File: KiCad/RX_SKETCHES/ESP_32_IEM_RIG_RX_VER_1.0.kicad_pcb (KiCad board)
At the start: 2 copper layers, 64 parts, among them J1 AudioJack3, J6 USB_C_Receptacle_USB2.0_16P, Q1 S8050, Q2 S8050, SW2 Interpolation Mode, SW3 DAC Soft Mute, SW4 ON/OFF, U1 PCM5102, U2 ESP32-WROOM-32U, U3 MAX97220AETE_T, U4 LM3940IMPX-3.3_NOPB, U5 CP2102C-Axx-xQFN24

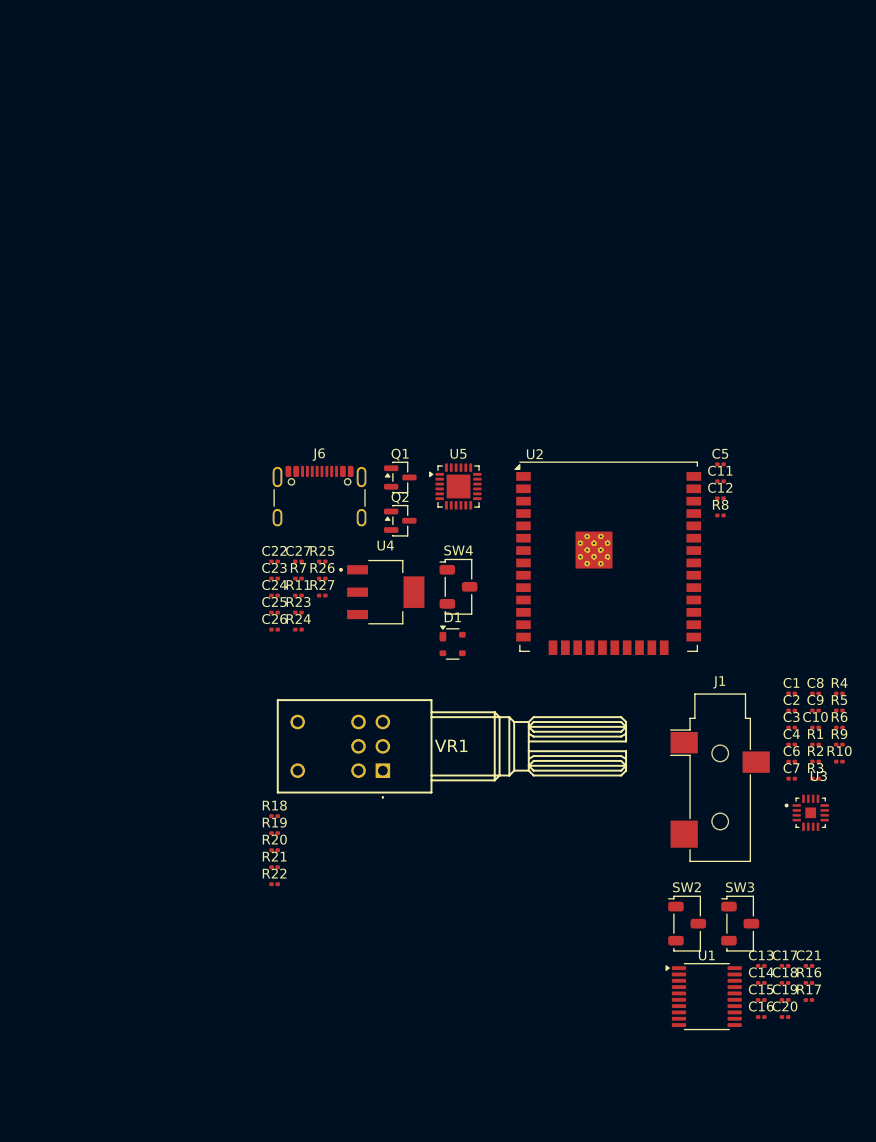
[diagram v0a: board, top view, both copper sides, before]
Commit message: RX v1: complete PCB layout, retune analog chain, fix ESD clamp placement
Brings the RX schematic and board up to a fabricable state. DRC is clean:
zero unconnected items, zero schematic-parity issues. The 16 remaining
violations are footprint-inherent and documented rather than worked around
(ESP32-WROOM thermal via array drilled 0.2 mm against a 0.3 mm rule, and
USB-C NPTH-to-pad spacing from the vendor land pattern).

Analog:
- Gain network populated at RF 4.7k / RIN 47k (-20 dB) rather than DNP 10k.
  Tames the PCM5102's 2.1 Vrms into sensitive IEMs, gives the 10k pot a
  4.7x loading ratio instead of 1:1, and lifts the coupling corner clear of
  the audible band.
- Coupling caps C1-C4 raised 0.47uF -> 1uF. Corner 7.2 Hz -> 3.4 Hz, and it
  halves the signal developed across the ceramic at 20 Hz, which is where
  Class-II dielectric distortion actually shows up.
- PCM5102 mode pins no longer float: 100k pulldowns on FLT and XSMT, with
  DEMP and FMT strapped to GND.

Power and protection:
- D1's third TVS channel moved off the switched +5V rail onto VBUS_RAW. An
  ESD clamp has to sit on the connector pin exposed to a finger; behind the
  power switch it disconnected exactly when the board is most likely to be
  handled. The off state is unaffected -- a TVS is open below its standoff
  voltage and SW4 still breaks the rail.
- All three slide switches now follow one rule: the open throw is the safe
  default (powered off / normal-latency filter / muted).

Housekeeping:
- C28 and mounting holes REF1-REF4 added to the schematic, clearing parity
  errors against parts that previously existed only on the PCB.
- Gain, loudness, and filter math written up in README.org with sources so
  the numbers can be re-derived; rationale logged in hardware_revisions.org.
- .gitignore now covers the editor .history/ directory and ESP-IDF build
  output, which were showing up as untracked noise.

Firmware and build artifacts are deliberately excluded from this commit.

Co-authored-b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
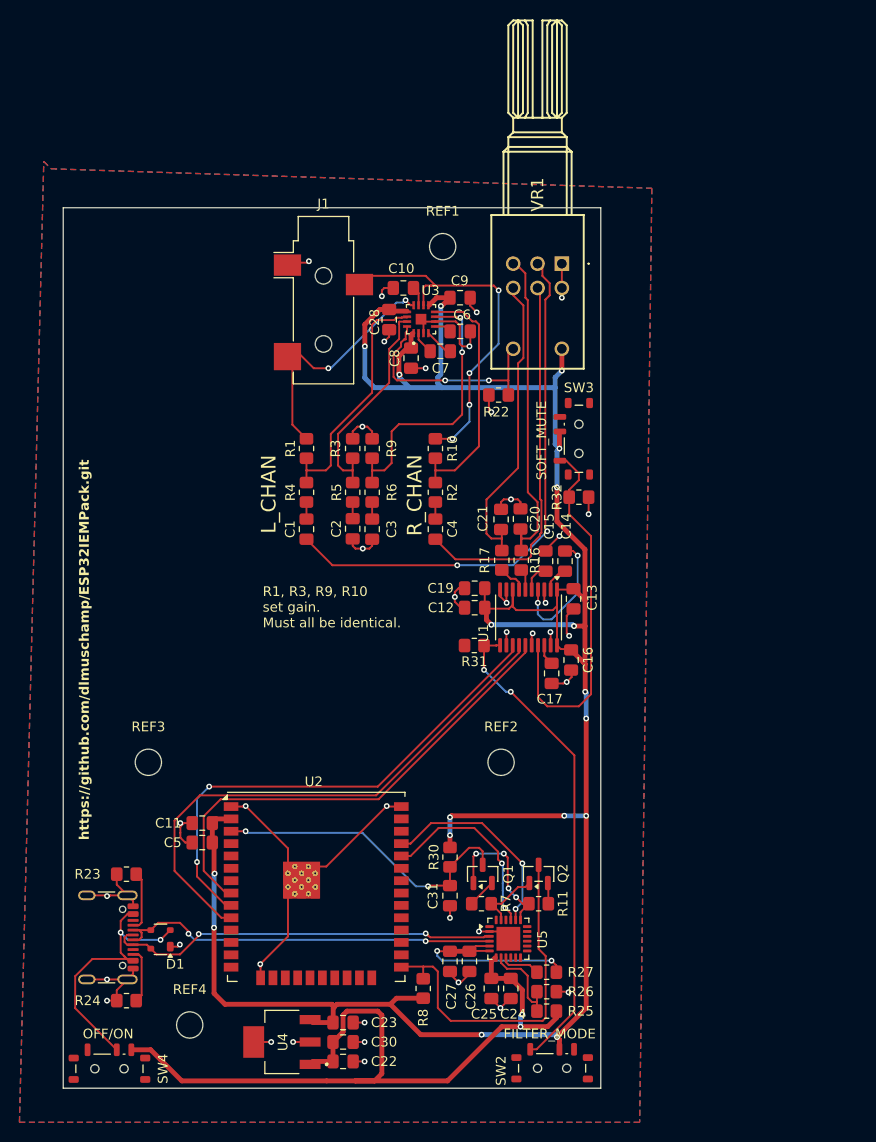
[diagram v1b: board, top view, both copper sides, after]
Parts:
- removed C18: 10u, Capacitor_SMD:C_0201_0603Metric
- removed R18, R20: 1k, Resistor_SMD:R_0201_0603Metric
- removed R19, R21: 10R, Resistor_SMD:R_0201_0603Metric
- added C28: 1u, Capacitor_SMD:C_0805_2012Metric_Pad1.18x1.45mm_HandSolder, F.Cu at (130.0, 50.0)
- added C30: 22u, Capacitor_SMD:C_0805_2012Metric_Pad1.18x1.45mm_HandSolder, F.Cu at (125.3, 124.2)
- added C31: 0.1u, Capacitor_SMD:C_0805_2012Metric_Pad1.18x1.45mm_HandSolder, F.Cu at (136.2, 109.2)
- added R30: 10k, Resistor_SMD:R_0805_2012Metric_Pad1.20x1.40mm_HandSolder, F.Cu at (136.2, 105.2)
- added R31: 100k, Resistor_SMD:R_0805_2012Metric_Pad1.20x1.40mm_HandSolder, F.Cu at (138.8, 83.5)
- added R32: 100k, Resistor_SMD:R_0805_2012Metric_Pad1.20x1.40mm_HandSolder, F.Cu at (149.5, 68.2)
- added REF1: MountingHole_2.7mm_M2.5, MountingHole:MountingHole_2.7mm_M2.5, F.Cu at (135.5, 42.5)
- added REF2: MountingHole_2.7mm_M2.5, MountingHole:MountingHole_2.7mm_M2.5, F.Cu at (141.5, 95.5)
- added REF3: MountingHole_2.7mm_M2.5, MountingHole:MountingHole_2.7mm_M2.5, F.Cu at (105.2, 95.5)
- added REF4: MountingHole_2.7mm_M2.5, MountingHole:MountingHole_2.7mm_M2.5, F.Cu at (109.5, 122.5)
- C1, C2, C3, C4: value 0.47u -> 1u; footprint Capacitor_SMD:C_0201_0603Metric -> Capacitor_SMD:C_0805_2012Metric_Pad1.18x1.45mm_HandSolder
- C10, C11, C13, C14, C15, C16, C17, C19, C20, C21, C23, C24, C25, C26, C27, C6, C7, C8, C9: footprint Capacitor_SMD:C_0201_0603Metric -> Capacitor_SMD:C_0805_2012Metric_Pad1.18x1.45mm_HandSolder
- C12: value 1u -> 10u; footprint Capacitor_SMD:C_0201_0603Metric -> Capacitor_SMD:C_0805_2012Metric_Pad1.18x1.45mm_HandSolder
- C22: value 22u -> 0.47u; footprint Capacitor_SMD:C_0201_0603Metric -> Capacitor_SMD:C_0805_2012Metric_Pad1.18x1.45mm_HandSolder
- C5: value 10u -> 22u; footprint Capacitor_SMD:C_0201_0603Metric -> Capacitor_SMD:C_0805_2012Metric_Pad1.18x1.45mm_HandSolder
- R1, R10, R3, R9: value 10k -> 4.7k; footprint Resistor_SMD:R_0201_0603Metric -> Resistor_SMD:R_0805_2012Metric_Pad1.20x1.40mm_HandSolder
- R11, R16, R17, R22, R23, R24, R25, R26, R27, R7, R8: footprint Resistor_SMD:R_0201_0603Metric -> Resistor_SMD:R_0805_2012Metric_Pad1.20x1.40mm_HandSolder
- R2, R4, R5, R6: value 10k -> 47k; footprint Resistor_SMD:R_0201_0603Metric -> Resistor_SMD:R_0805_2012Metric_Pad1.20x1.40mm_HandSolder
- SW2: value Interpolation Mode -> FILTER_MODE; footprint Button_Switch_SMD:Nidec_Copal_CAS-120A -> Button_Switch_SMD:SW_SPDT_Shouhan_MSK12C02
- SW3: value DAC Soft Mute -> SOFT_MUTE; footprint Button_Switch_SMD:Nidec_Copal_CAS-120A -> Button_Switch_SMD:SW_SPDT_Shouhan_MSK12C02
- SW4: footprint Button_Switch_SMD:Nidec_Copal_CAS-120A -> Button_Switch_SMD:SW_SPDT_Shouhan_MSK12C02
- moved C5 65.9 mm to (110.8, 103.8), turned to 180 degrees
- moved U3 64.6 mm to (133.3, 50.0), turned to 90 degrees
- moved J1 63.8 mm to (123.2, 48.0)
- moved C11 63.8 mm to (110.8, 101.8), turned to 180 degrees
- moved C10 61.9 mm to (131.5, 46.8), turned to 180 degrees
- moved SW4 61.2 mm to (101.2, 127.0)
- moved R1 60.5 mm to (121.5, 63.2), turned to 90 degrees
- moved R4 58.6 mm to (121.5, 67.8), turned to 90 degrees
- moved R3 58.4 mm to (126.2, 63.2), turned to 90 degrees
- moved C20 58.0 mm to (143.5, 70.5), turned to 90 degrees
- moved R8 57.4 mm to (133.5, 118.8), turned to 90 degrees
- moved C7 56.9 mm to (135.2, 53.2)
- moved R9 56.9 mm to (128.2, 63.2), turned to -90 degrees
- moved C9 56.0 mm to (137.3, 47.8)
- moved C6 55.8 mm to (137.3, 51.2)
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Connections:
- net /Amp/AMP_OUT_L renamed Net-(U3-OUTL)
- net /Amp/AMP_OUT_R renamed Net-(U3-OUTR)
- net /DAC/DIN renamed /DAC/DOUT
- net Net-(SW2-C) renamed /DAC/FLT_SEL
- C12 pad 1: GND -> +3V3
- C12 pad 2: /ESP Reciever/ESP_EN -> GND
- D1 pad 2: +5V -> /Power Management/VBUS_RAW
- J6 pad A4: Net-(SW4-B) -> /Power Management/VBUS_RAW
- J6 pad A9: Net-(SW4-B) -> /Power Management/VBUS_RAW
- J6 pad B4: Net-(SW4-B) -> /Power Management/VBUS_RAW
- J6 pad B9: Net-(SW4-B) -> /Power Management/VBUS_RAW
- R8 pad 2: /ESP Reciever/ESP_EN -> /ESP Reciever/ESP_IO0
- SW3 pad 1: unconnected-(SW3-C-Pad1) -> /DAC/XSMT_SEL
- SW3 pad 3: Net-(SW3-A) -> unconnected-(SW3-A-Pad3)
- SW4 pad 2: Net-(SW4-B) -> /Power Management/VBUS_RAW
- U1 pad 10: unconnected-(U1-DEMP-Pad10) -> GND
- U1 pad 16: unconnected-(U1-FMT-Pad16) -> GND
- U1 pad 17: Net-(SW3-A) -> /DAC/XSMT_SEL
- U2 pad 2: GND -> +3V3
- VR1 pad 3: /Volume Control/PRE_POT_IN_L -> /DAC/DAC_OUT_L
- VR1 pad 6: /Volume Control/PRE_POT_IN_R -> /DAC/DAC_OUT_R
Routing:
- net +3V3: track 0.00 -> 249.3 mm, vias 0 -> 18
- net GND: track 0.00 -> 129.9 mm, vias 0 -> 39
- net +5V: track 0.00 -> 79.3 mm, vias 0 -> 2
- net /DAC/DOUT: track 0.00 -> 56.3 mm
- net /Amp/POST_POT_IN_L: track 0.00 -> 55.8 mm, vias 0 -> 2
- net /DAC/BCK: track 0.00 -> 52.1 mm, vias 0 -> 2
- net /DAC/LRCLK: track 0.00 -> 50.1 mm
- net /DAC/FLT_SEL: track 0.00 -> 49.6 mm, vias 0 -> 2
- net Net-(U5-D+): track 0.00 -> 40.8 mm, vias 0 -> 2
- net Net-(U5-D-): track 0.00 -> 40.4 mm, vias 0 -> 2
- net /Amp/POST_POT_IN_R: track 0.00 -> 39.2 mm
- net /DAC/XSMT_SEL: track 0.00 -> 38.2 mm
- net Net-(U3-OUTR): track 0.00 -> 37.3 mm, vias 0 -> 4
- net /ESP Reciever/ESP_IO0: track 0.00 -> 36.9 mm
- net /DAC/DAC_OUT_L: track 0.00 -> 34.8 mm
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- added copper zone on B.Cu, net GND
- added copper zone on F.Cu, net GND
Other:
- board outline added: 55.2 x 90.5 mm
- board text added: "FILTER_MODE"
- board text added: "L_CHAN"
- board text added: "OFF/ON"
- board text added: "R1, R3, R9, R10 set gain. Must all be identical."
- board text added: "R10"
- board text added: "R_CHAN"
- board text added: "SOFT_MUTE"
- board text added: "https://github.com/dlmuschamp/ESP32IEMPack.git"
